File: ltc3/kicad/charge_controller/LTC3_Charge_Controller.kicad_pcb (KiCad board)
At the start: 4 copper layers, 91.3 x 82.5 mm, 112 parts, among them P1 PV_IN, P2 LAB_IN, P3 S2BPHKS, Q1 ZVN4525E6, Q2 BSC028N06NS, Q3 BSC028N06NS, Q4 BSC028N06NS, Q5 BSC028N06NS, Q6 ZVP3310F, Q7 MMBT5550L, U1 PI2127, U2 PI2127, U3 LT8490, U4 LTC2990

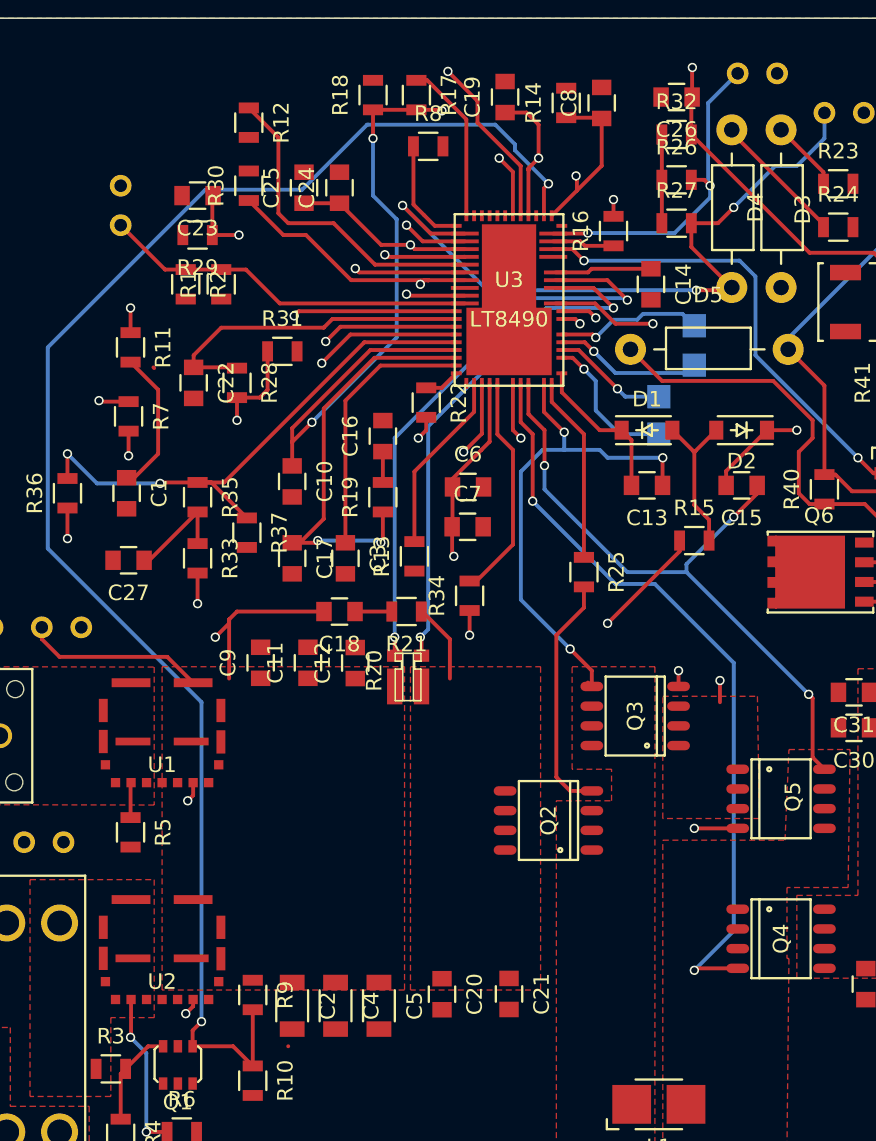
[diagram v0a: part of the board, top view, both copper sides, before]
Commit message: LTC3: Charge Controller Layout
Noticed some unconnected nets that were NOT unconnected GND nodes due to
lack of via stiching.  Have connected these nets.
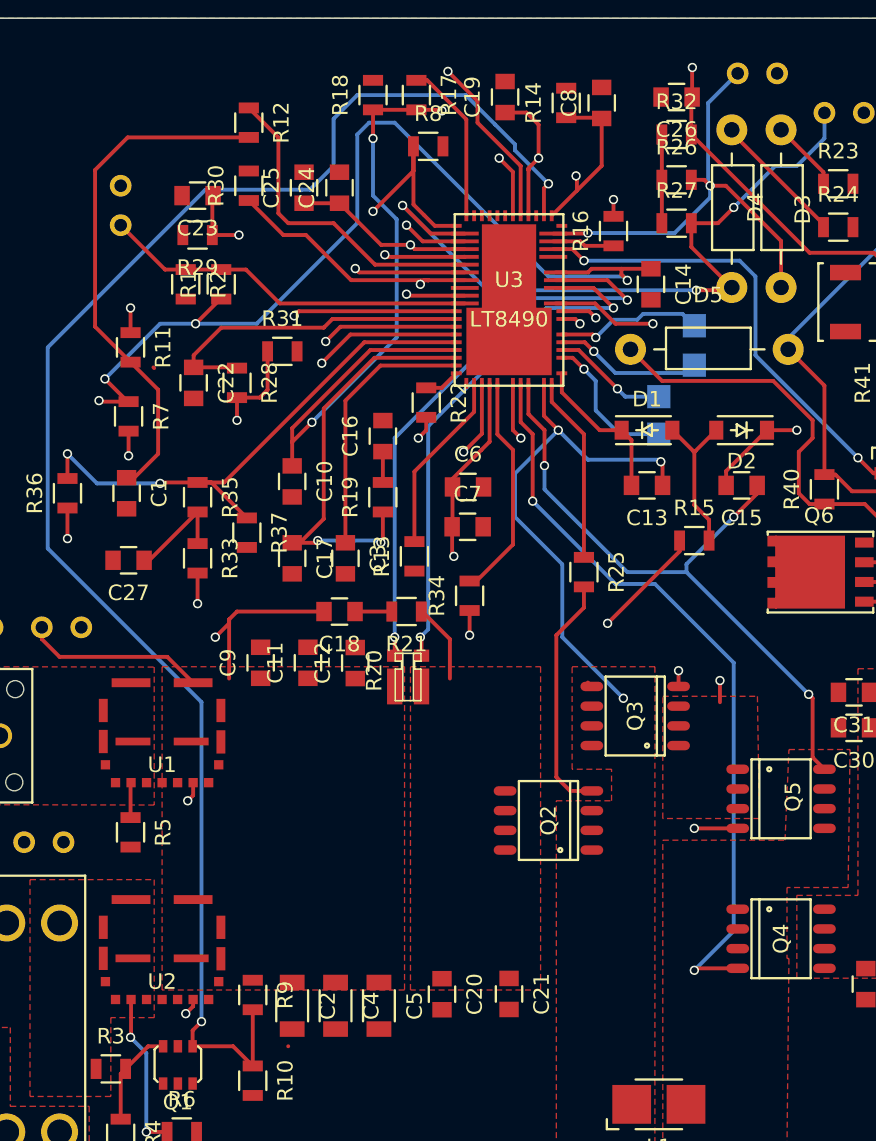
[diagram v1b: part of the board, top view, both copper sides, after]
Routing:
- net VIN: track 50.5 -> 103.9 mm, vias 2 -> 5
- net Net-(C1-Pad1): track 9.31 -> 33.4 mm
- net Net-(R11-Pad1): track 44.2 -> 61.6 mm, vias 3 -> 4
- net Net-(D3-Pad2): track 21.7 -> 30.7 mm
- net Net-(Q1-Pad1): track 99.6 -> 102.9 mm
- net /SW1: track 32.8 -> 34.1 mm

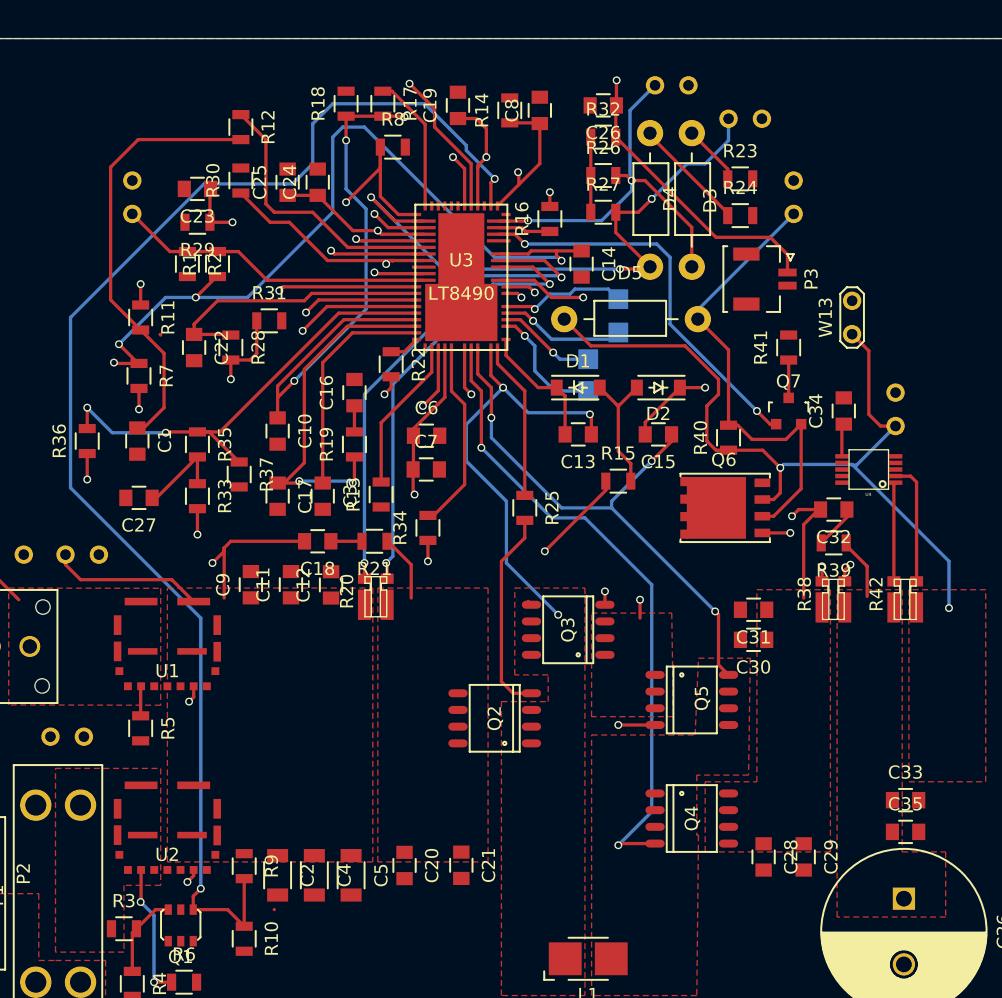
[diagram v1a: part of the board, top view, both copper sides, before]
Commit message: LTC3: "Via stitching" for LT8490
Connected all the ground nodes through KiCads "via stitching methods."
More vias to come, but for now all nodes should be connected.
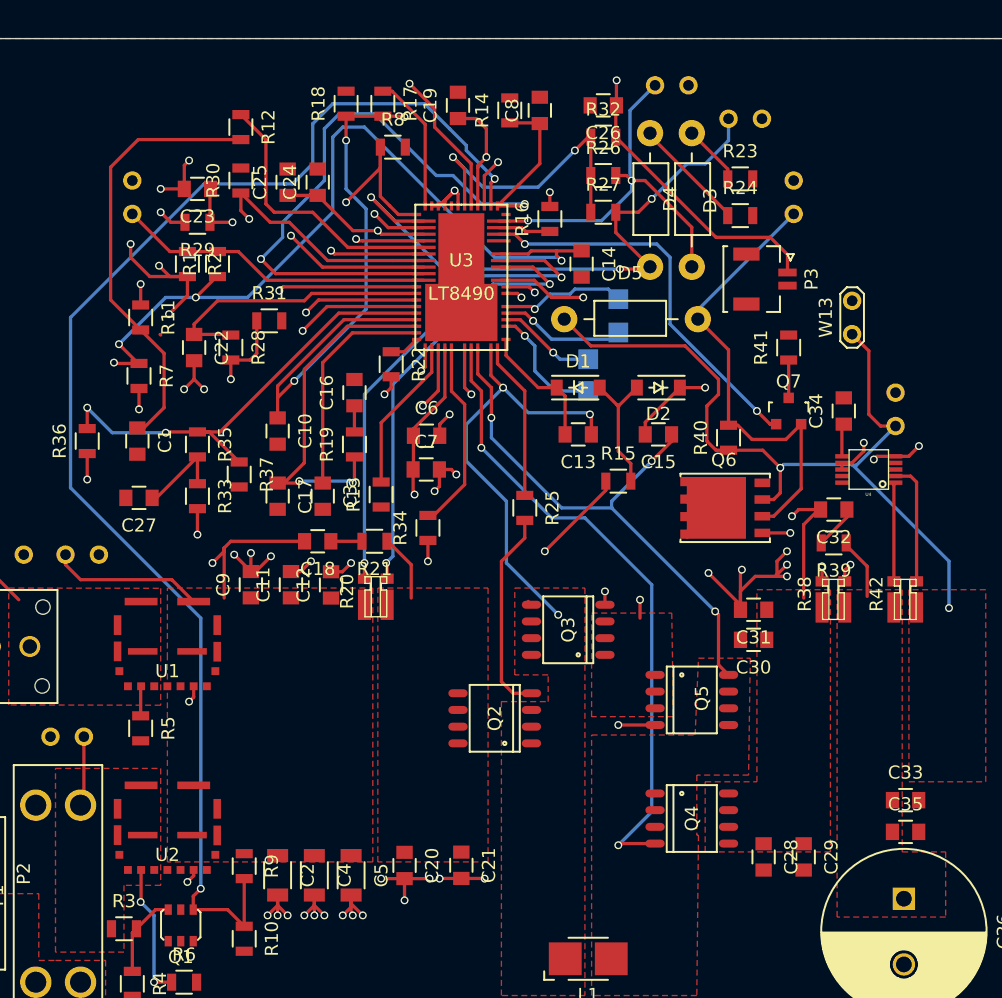
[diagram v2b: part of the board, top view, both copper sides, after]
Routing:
- net GND: track 2.42 -> 107.4 mm, vias 2 -> 44
- net Net-(Q7-Pad1): track 59.1 -> 100.0 mm
- net Net-(C8-Pad1): track 29.7 -> 55.4 mm
- net +3V3: track 49.4 -> 62.4 mm, vias 3 -> 4
- net Net-(F1-Pad2): track 0.00 -> 5.31 mm
- net Net-(C6-Pad1): track 62.7 -> 63.3 mm

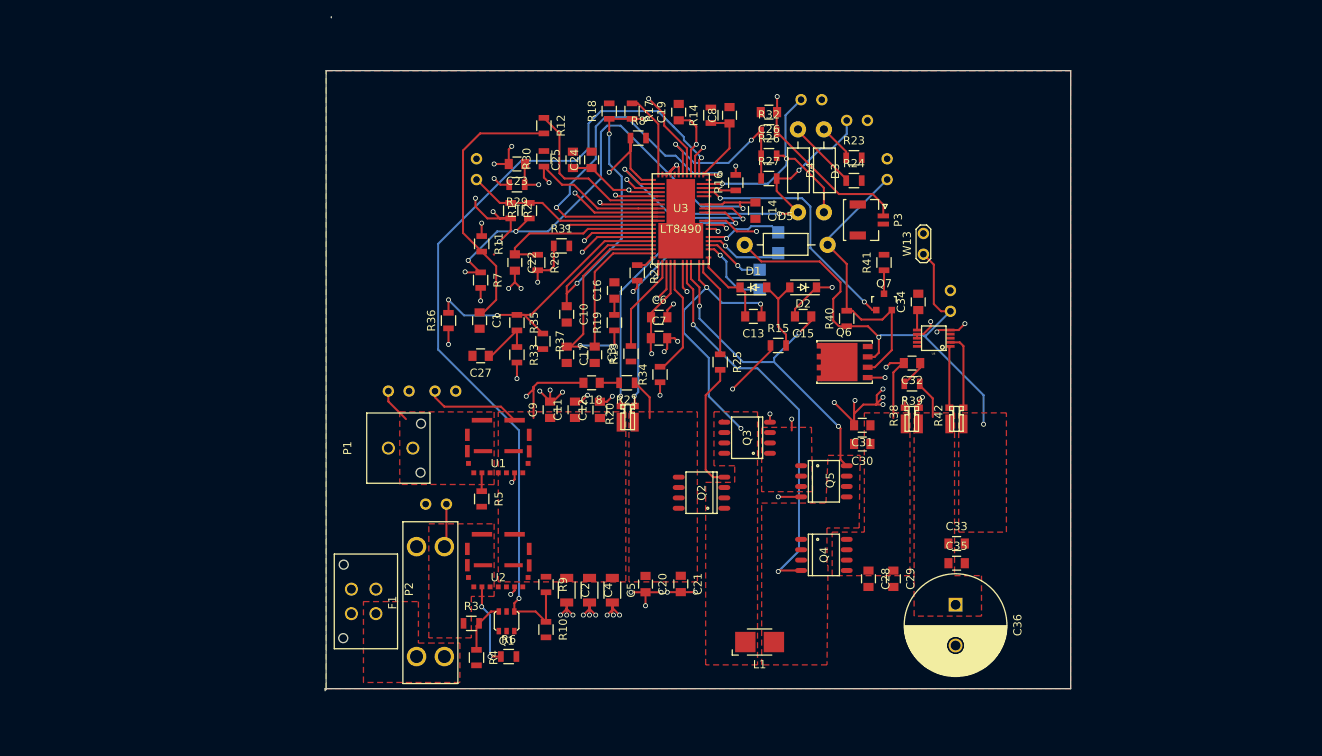
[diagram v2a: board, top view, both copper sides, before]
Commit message: LTC3: LT8490 Layout
Some final changes and preparation for LT8490 layout.
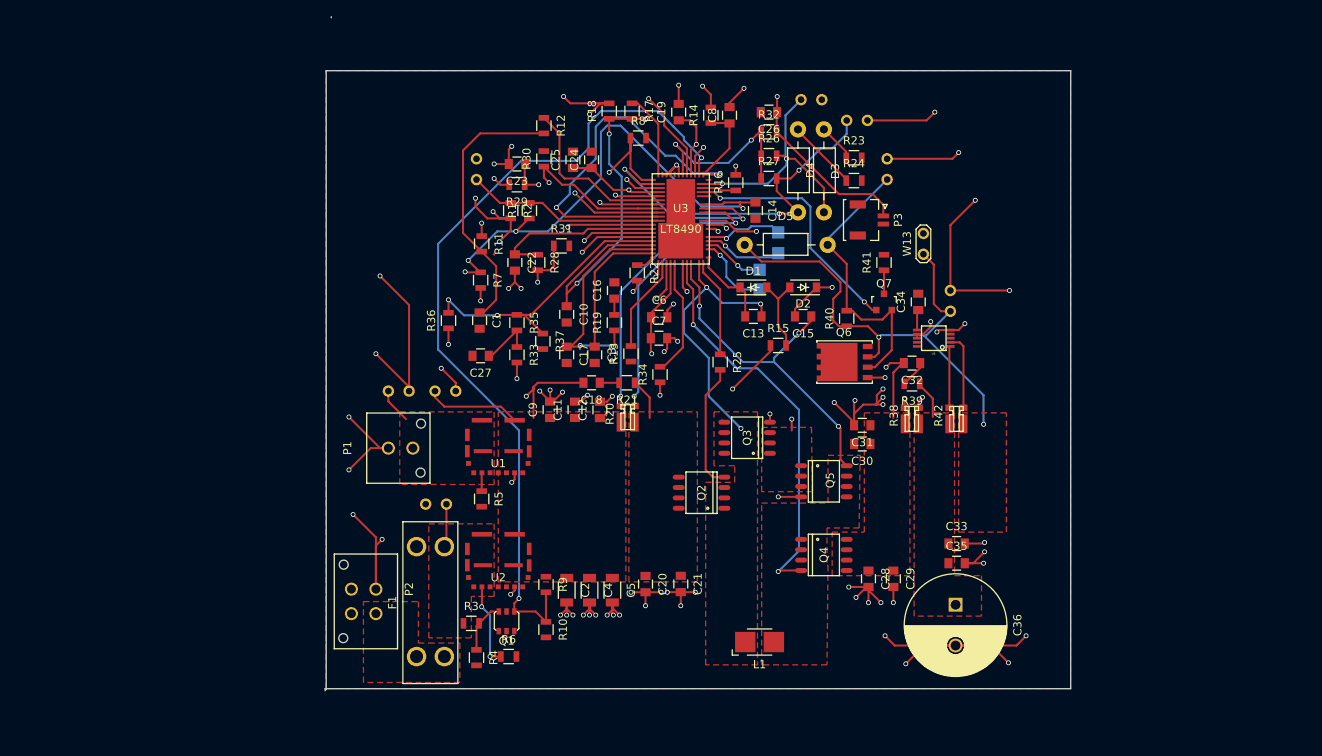
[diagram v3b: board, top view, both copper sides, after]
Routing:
- net GND: track 107.4 -> 270.5 mm, vias 44 -> 73

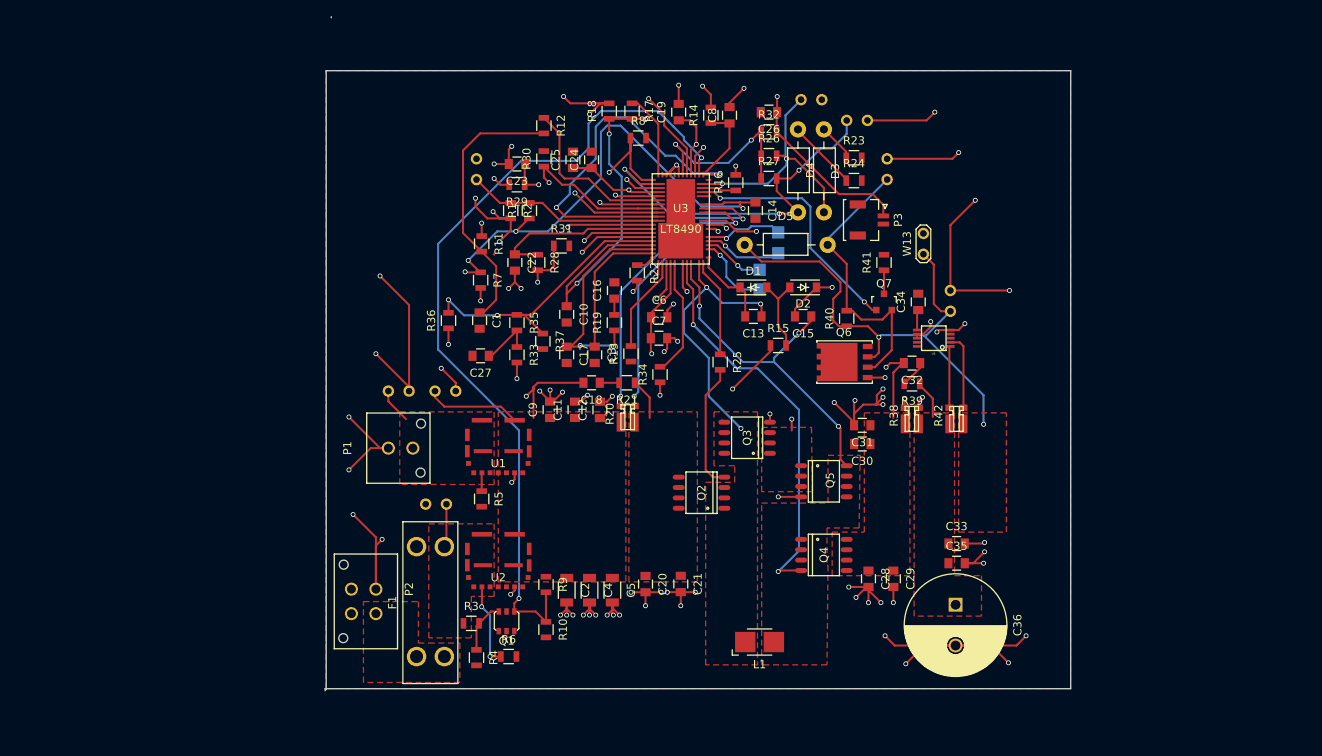
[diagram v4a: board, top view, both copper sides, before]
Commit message: LTC3: Reworking Charge Controller Layout
- Assigned correct footprints to LEDs, Fuse, output connector
- Reworked high current polygons
- Added mounting holes

Still more work to be done.
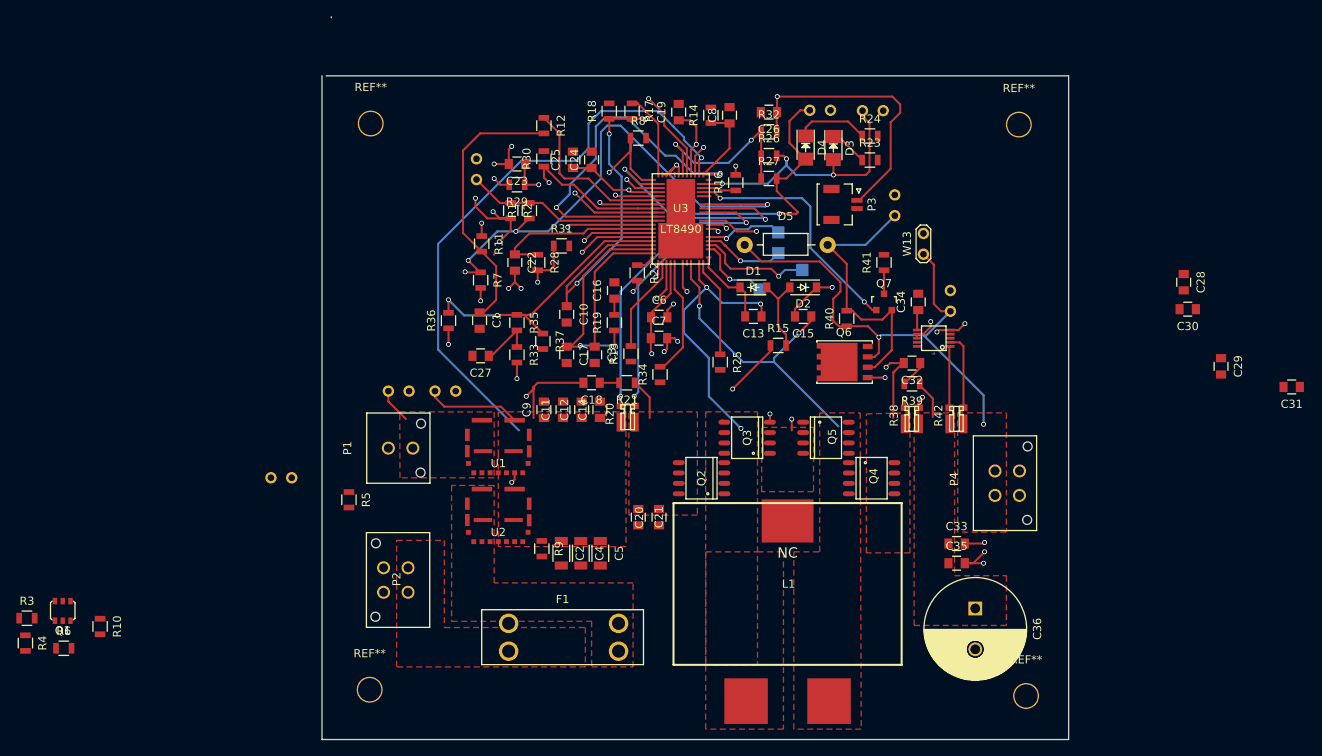
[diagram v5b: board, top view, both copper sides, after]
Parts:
- added P4: MicroFit header, Connectors_Molex:Molex_Microfit3_Header_02x02_Straight_43045-0428, F.Cu at (177.7, 113.6)
- added REF**: MountingHole_0.1120in_#4, LTC3:MountingHole_0.1120in_number4, F.Cu at (101.1, 137.4)
- added REF**: MountingHole_0.1120in_#4, LTC3:MountingHole_0.1120in_number4, F.Cu at (181.5, 138.2)
- added REF**: MountingHole_0.1120in_#4, LTC3:MountingHole_0.1120in_number4, F.Cu at (180.6, 68.2)
- added REF**: MountingHole_0.1120in_#4, LTC3:MountingHole_0.1120in_number4, F.Cu at (101.2, 68.1)
- D3: value LED -> GREEN; footprint Choke_Axial_ThroughHole:Choke_Horizontal_RM10mm -> LEDs:LED_1206
- D4: value LED -> RED; footprint Choke_Axial_ThroughHole:Choke_Horizontal_RM10mm -> LEDs:LED_1206
- L1: footprint Inductors:Inductor_1212 -> LTC3:Coilcraft_SER2900
- P1: value PV_IN -> MicroFit header
- P2: value LAB_IN -> MicroFit header
- moved R4 55.3 mm to (58.9, 131.7)
- moved R10 54.6 mm to (68.1, 129.7)
- moved R6 54.5 mm to (63.6, 132.3)
- moved R3 54.4 mm to (59.1, 128.7)
- moved Q1 54.4 mm to (63.5, 127.8)
- moved C28 53.0 mm to (200.8, 87.5)
- moved C31 52.8 mm to (214.0, 100.3)
- moved C29 47.8 mm to (205.4, 97.8)
- moved C30 43.1 mm to (201.3, 90.8)
- moved C14 30.9 mm to (129.3, 103.1), turned to 90 degrees
- moved W1 19.2 mm to (89.0, 111.5)
- moved F1 16.7 mm to (124.7, 131.0), turned to 0 degrees
- moved R5 16.3 mm to (98.6, 114.1)
- moved Q4 11.1 mm to (162.6, 111.5)
- moved C21 8.60 mm to (136.5, 116.3)
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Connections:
- net VBATT renamed Net-(D5-Pad1)
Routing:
- net GND: track 270.5 -> 67.0 mm, vias 73 -> 22
- net /TG2: track 48.9 -> 0.00 mm, vias 2 -> 0
- net Net-(Q1-Pad1): track 102.9 -> 72.5 mm, vias 2 -> 1
- net /BG2: track 28.9 -> 0.00 mm, vias 2 -> 0
- net /TG1: track 15.6 -> 0.00 mm
- net Net-(C26-Pad1): track 53.8 -> 65.2 mm
- net Net-(R6-Pad1): track 10.3 -> 0.00 mm, vias 2 -> 0
- net Net-(U3-Pad36): track 7.50 -> 14.0 mm
- net Net-(Q1-Pad3): track 6.39 -> 0.00 mm
- net Net-(R20-Pad4): track 37.9 -> 43.5 mm
- net Net-(F1-Pad2): track 5.31 -> 0.00 mm
- net /SW2: track 42.5 -> 37.2 mm, vias 3 -> 2
- net Net-(D3-Pad2): track 30.7 -> 35.3 mm, vias 2 -> 3
- net VIN: track 103.9 -> 107.3 mm
- net Net-(R20-Pad3): track 34.4 -> 37.0 mm
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- removed copper zone on F.Cu, net GND
- removed copper zone on Ground.Plane, net GND
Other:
- board size 91.3 x 82.5 mm -> 91.4 x 88.5 mm
